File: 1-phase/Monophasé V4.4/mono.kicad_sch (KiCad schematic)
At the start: 75 parts, among them IC1 LM358, IC2 ATmega328-P, J1 UnregDC, J10 D10, J11 D11, J12 D12, J13 D13, J14 D2, J15 D3, J16 D4, J17 D5, J18 D6, J19 D7, J2 D2, J20 D8, J21 D9, J22 D10, J23 D11, J24 D12, J25 D13, J26 RESET, J27 FTDI, J28 +5V, J29 +5V, J3 D3, J30 regDC, J4 D4, J5 D5, J6 D6, J7 D7, J8 D8, J9 D9, U1 DS18B20, X1 16MHz

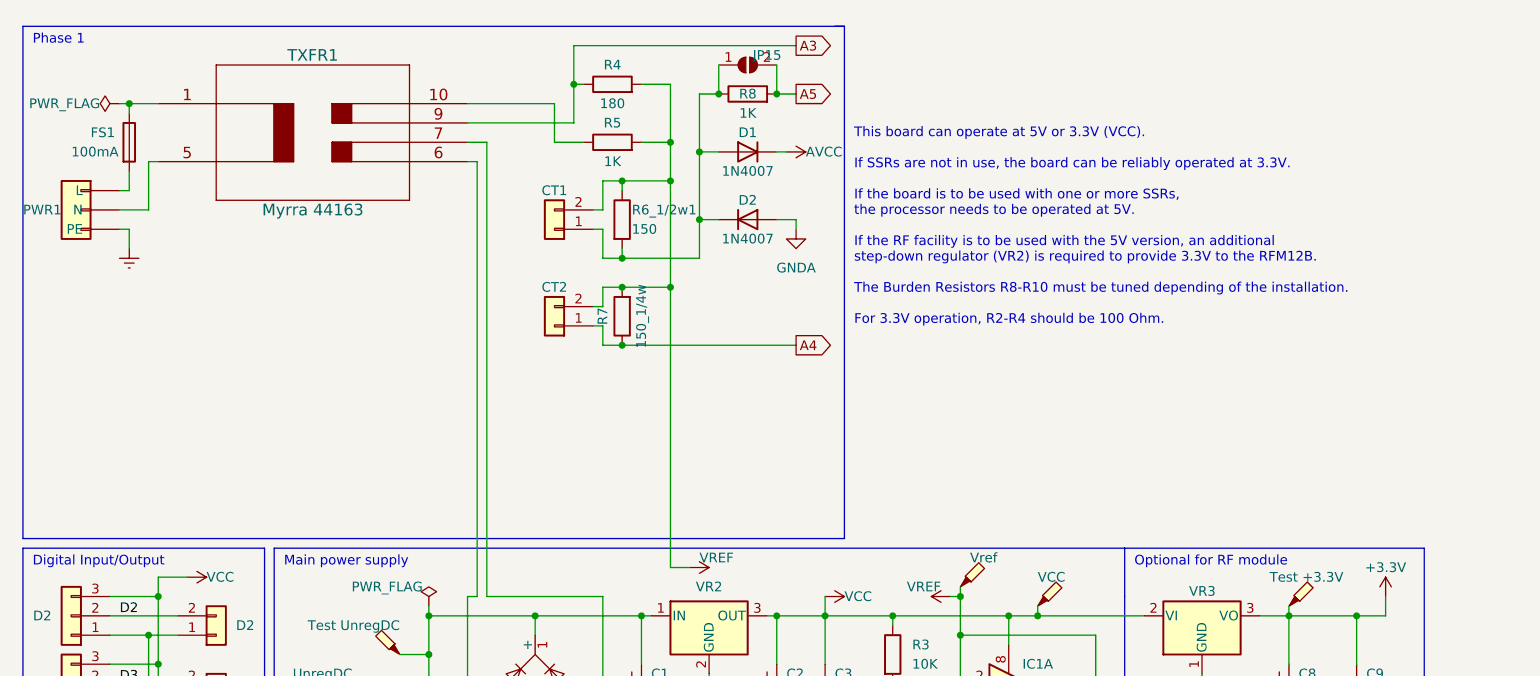
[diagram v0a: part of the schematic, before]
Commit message: Led status RF
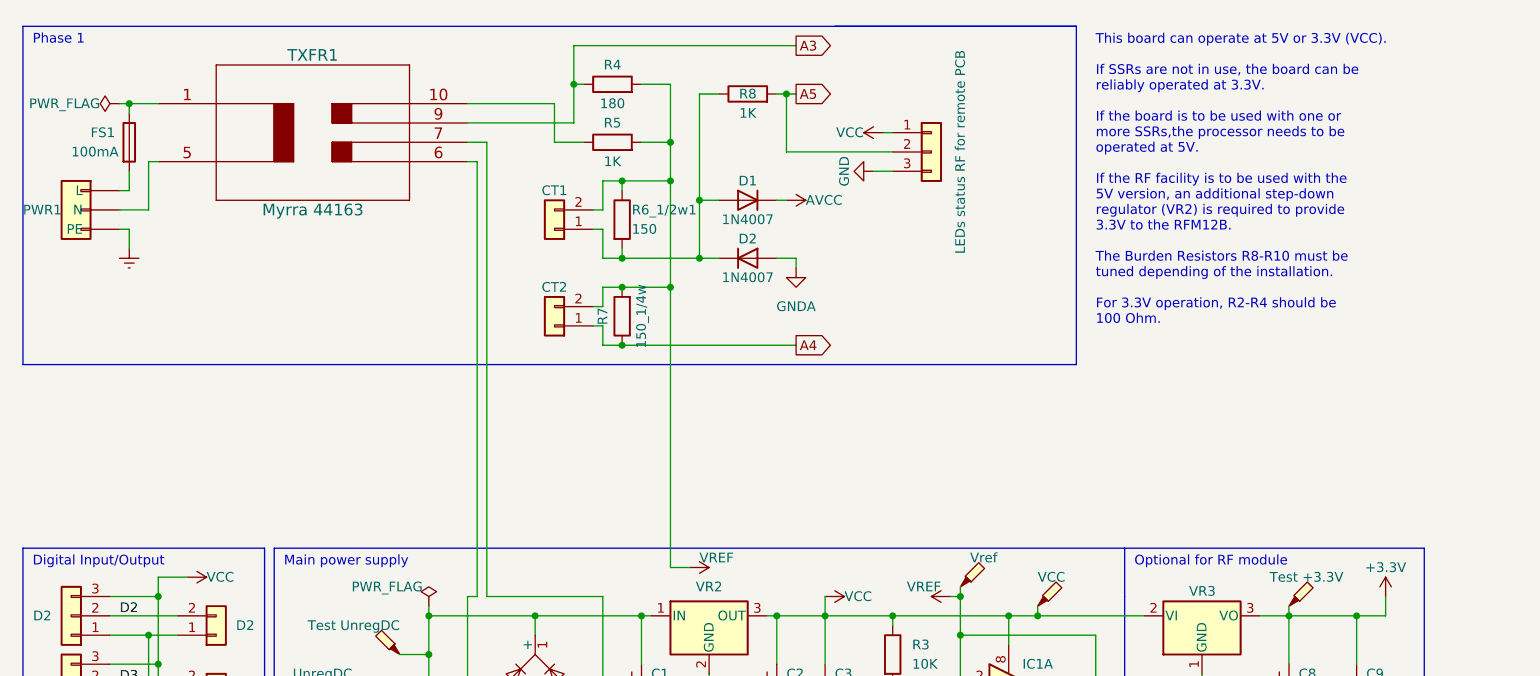
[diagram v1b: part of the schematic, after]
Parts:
- removed JP15: SolderJumper_2_Open, Jumper:SolderJumper-2_P1.3mm_Open_TrianglePad1.0x1.5mm, symbol Jumper:SolderJumper_2_Open
- added J31: LEDs status RF for remote PCB, Library:Molex_SL_171971-0003_1x03_P2.54mm_Vertical, symbol Connector_Generic:Conn_01x03
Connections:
- net A5: now also J31.2 (Pin_2)
- net GND: now also J31.3 (Pin_3)
- net VCC: now also J31.1 (Pin_1)
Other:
- note added: "This board can operate at 5V or 3.3V (VCC). If SSRs are not in use, the board can be reliably operated at 3.3V. If the board is to be used with one or more SSRs,the processor needs to be operated at 5V. If the RF facility is to be used with the 5V version, an additional step-down regulator (VR2) is required to provide 3.3V to the RFM12B. The Burden Resistors R8-R10 must be tuned depending of the 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"
- note removed: "This board can operate at 5V or 3.3V (VCC). If SSRs are not in use, the board can be reliably operated at 3.3V. If the board is to be used with one or more SSRs, the processor needs to be operated at 5V. If the RF facility is to be used with the 5V version, an additional step-down regulator (VR2) is required to provide 3.3V to the RFM12B. The Burden Resistors R8-R10 must be tuned depending of the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"
- moved on the sheet: D1, D2
